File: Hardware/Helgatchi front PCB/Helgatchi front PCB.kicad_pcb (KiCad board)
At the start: 2 copper layers, 50 x 80 mm, 34 parts, among them J1 BATTERY, J2 SCREEN, M1 MOTOR, Q1 NMOS, SW1 LEFT BUTTON, SW2 CENTER BUTTON, SW3 RIGHT BUTTON, U1 XIAO ESP32-S3

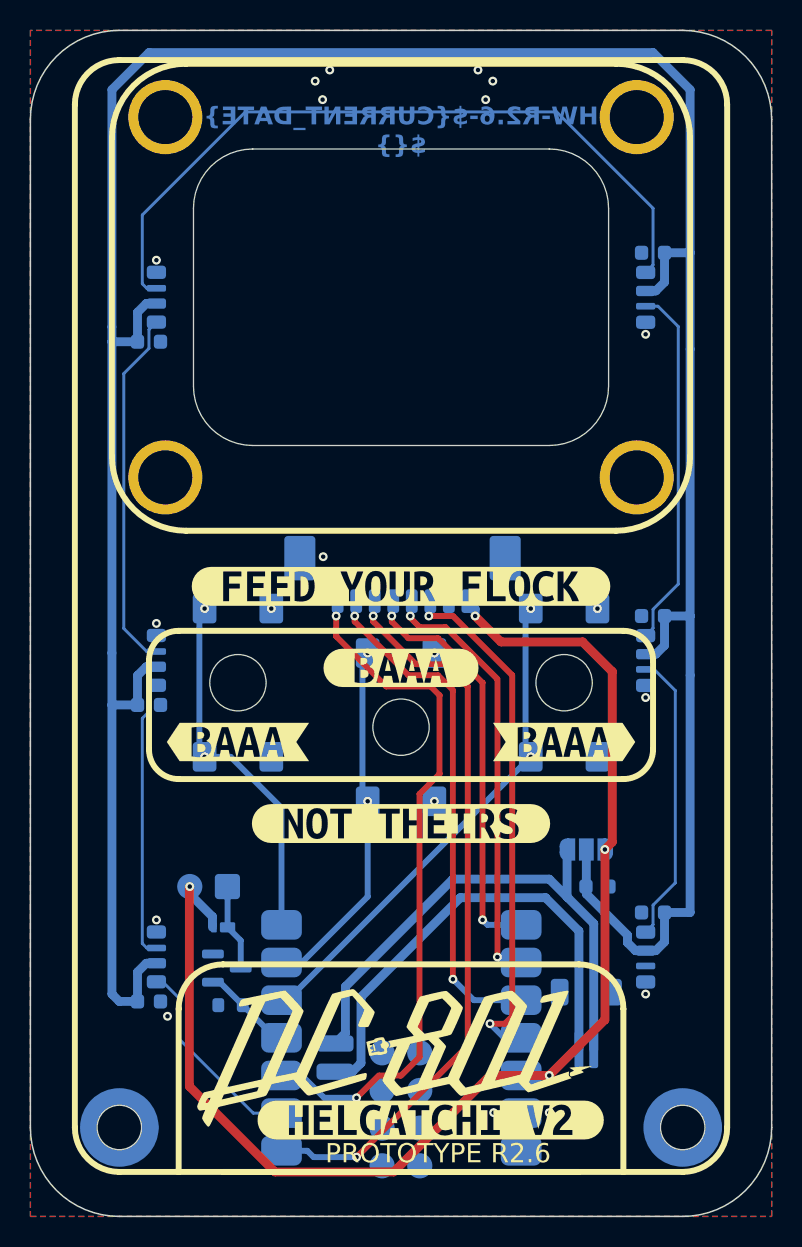
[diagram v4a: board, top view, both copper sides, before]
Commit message: R2.7
- Shifted buttons up a tiny bit
- Made room for the vibration motor to be adhered to the PCB
- Enlarged vibration motor pads for easier hand soldering
- Removed LED voltage selector (now 3.3v)
- Removed unused pins from schematic and ESP32 footprint
- Added a keepout area under ESP32
- Replaced +BATT trace
- Removed -BATT trace, tied to GND
- Added keepout around button GND vias, to prevent heat soak during soldering
- Scooted ESP back a little bit to make room for assembly
- Adjusted front silkscreen
- Swapped buttons to two GPIO Diode matrix
- Added VSENSE + resistors and capacitor
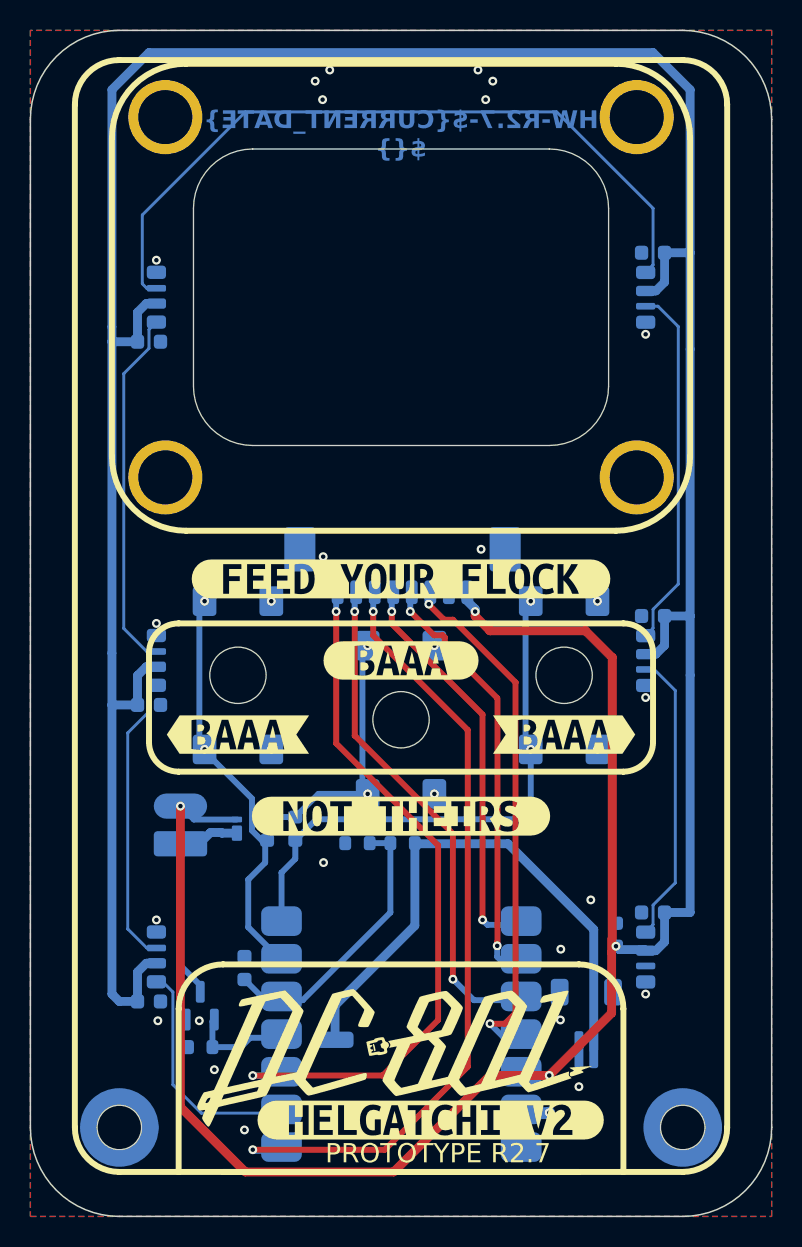
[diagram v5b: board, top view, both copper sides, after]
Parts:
- removed JP1: LEDs, Jumper:SolderJumper-3_P1.3mm_Open_RoundedPad1.0x1.5mm_NumberLabels
- added C8: 100nF, Capacitor_SMD:C_0603_1608Metric, B.Cu at (153.4, 121.7)
- added D8: D_Small, Diode_SMD:D_0603_1608Metric, B.Cu at (156.9, 112.3)
- added D9: D_Small, Diode_SMD:D_0603_1608Metric, B.Cu at (155.0, 112.3)
- added R2: 100kΩ, Resistor_SMD:R_0603_1608Metric, B.Cu at (164.1, 113.3)
- added R3: 100kΩ, Resistor_SMD:R_0603_1608Metric, B.Cu at (161.1, 113.3)
- moved D1 6.72 mm to (152.9, 112.3), turned to -90 degrees
- moved M1 5.46 mm to (149.1, 110.8), turned to 180 degrees
- moved R1 3.49 mm to (150.5, 127.1)
- moved C7 3.48 mm to (178.5, 119.5), turned to 90 degrees
- moved Q1 3.11 mm to (150.5, 124.3), turned to 90 degrees
- moved J2 0.60 mm to (164.1, 94.0)
- moved SW1 0.50 mm to (153.0, 102.0)
- moved SW2 0.50 mm to (164.0, 105.0)
- moved SW3 0.50 mm to (175.0, 102.0)
- moved kibuzzard-6976EA3A 0.50 mm to (175.0, 106.0)
- moved kibuzzard-6976EA47 0.50 mm to (153.0, 106.0)
- moved kibuzzard-6976EEFC 0.50 mm to (164.0, 95.5)
- moved kibuzzard-6976EF0C 0.50 mm to (164.0, 111.5)
- moved kibuzzard-69862DFC 0.50 mm to (164.0, 101.0)
- moved U1 0.25 mm to (164.0, 126.2)
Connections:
- C1 pad 2: LED_PWR -> +3.3V
- C2 pad 2: LED_PWR -> +3.3V
- C3 pad 2: LED_PWR -> +3.3V
- C4 pad 2: LED_PWR -> +3.3V
- C5 pad 2: LED_PWR -> +3.3V
- C6 pad 2: LED_PWR -> +3.3V
- C7 pad 1: LED_PWR -> +3.3V
- D2 pad 2: LED_PWR -> +3.3V
- D3 pad 2: LED_PWR -> +3.3V
- D4 pad 2: LED_PWR -> +3.3V
- D5 pad 2: LED_PWR -> +3.3V
- D6 pad 2: LED_PWR -> +3.3V
- D7 pad 2: LED_PWR -> +3.3V
- J1 pad 1: -BATT -> GND
- SW1 pad 2: BUTTON_LEFT -> BUTTONS_1
- SW2 pad 2: BUTTON_CENTER -> Net-(D8-K)
- SW3 pad 2: BUTTON_RIGHT -> BUTTONS_2
- U1 pad 5: BUTTON_RIGHT -> VSENSE
- U1 pad 6: BUTTON_CENTER -> BUTTONS_1
- U1 pad 7: BUTTON_LEFT -> BUTTONS_2
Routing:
- net +3.3V: track 89.3 -> 288.8 mm
- net LED_PWR: track 198.0 -> 0.00 mm
- net BUTTONS_2: track 0.00 -> 36.8 mm, vias 0 -> 2
- net BUTTON_RIGHT: track 33.9 -> 0.00 mm, vias 2 -> 0
- net -BATT: track 32.9 -> 0.00 mm
- net BUTTONS_1: track 0.00 -> 27.9 mm, vias 0 -> 2
- net BUTTON_LEFT: track 24.8 -> 0.00 mm, vias 2 -> 0
- net BUTTON_CENTER: track 24.4 -> 0.00 mm, vias 2 -> 0
- net VSENSE: track 0.00 -> 18.9 mm
- net Net-(D8-K): track 0.00 -> 17.7 mm, vias 0 -> 2
- net Net-(D1-A): track 5.96 -> 14.7 mm
- net SPI_DC: track 49.8 -> 53.0 mm
- net LED_CONTROL: track 13.7 -> 15.9 mm
- net GND: track 0.00 -> 2.01 mm, vias 16 -> 24
- net +BATT: track 36.9 -> 38.3 mm
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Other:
- board text added: "MOTOR"

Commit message: Update Helgatchi front PCB.kicad_pcb
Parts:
- moved C8 1.13 mm to (152.6, 122.5), turned to 0 degrees
- moved M1 0.62 mm to (148.5, 110.8)
- moved D1 0.43 mm to (152.5, 112.3)
- moved D9 0.36 mm to (154.6, 112.3)
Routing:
- net GND: vias 24 -> 25

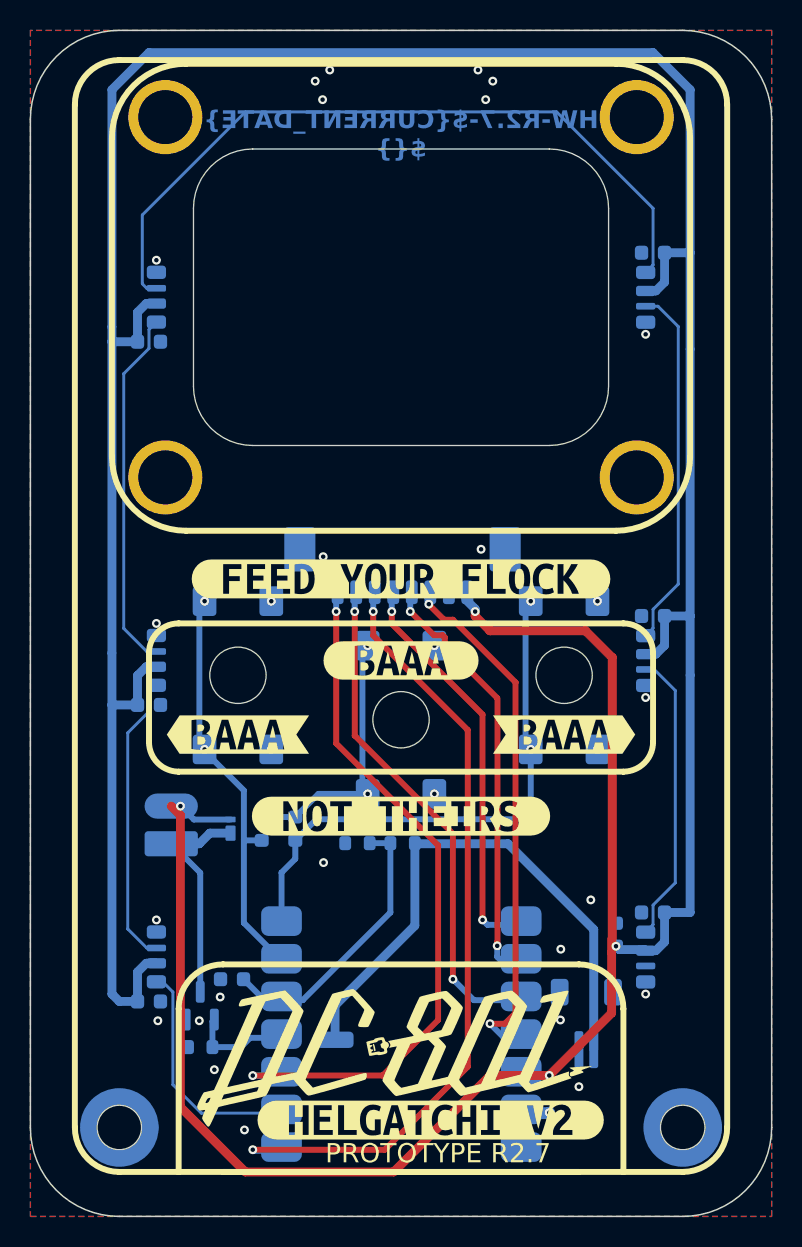
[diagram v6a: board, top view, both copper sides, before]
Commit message: Wrap up R2.7
- Added voltage sensing
- made room for Vibration buzzer
- added SMD M2 nut
- swapped flyback diode
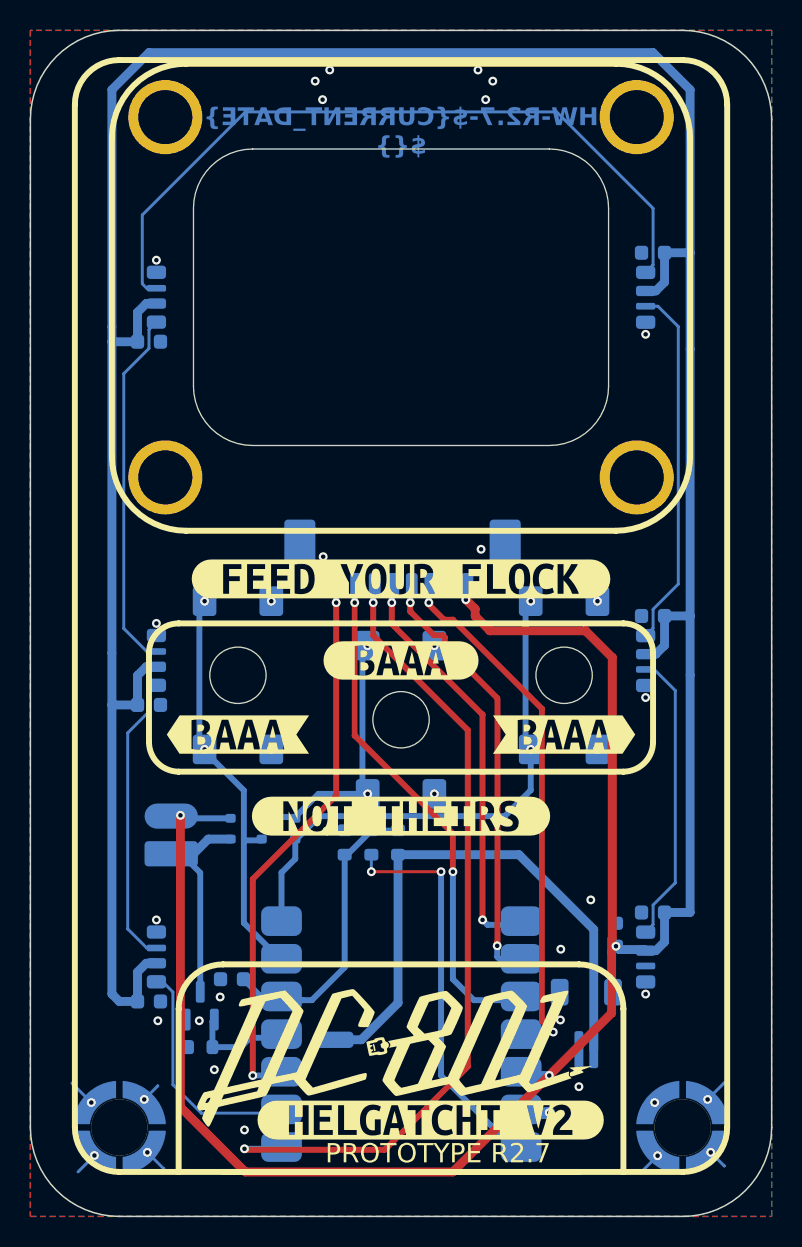
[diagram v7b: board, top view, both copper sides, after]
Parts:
- added R4: 100kΩ, Resistor_SMD:R_0603_1608Metric, B.Cu at (162.0, 113.3)
- D1: footprint SDM2U30CSP:SDM2U30CSP -> Diode_SMD:D_SOD-523
- D8, D9: value D_Small -> D_Schottky; footprint Diode_SMD:D_0603_1608Metric -> Diode_SMD:D_SOD-523
- H1, H2: value M2 -> SMTSOM225BTR; footprint Mounting_Wuerth:Mounting_Wuerth_WA-SMSI-M2_H8mm_9774080243 -> SMTSOM225BTR:SMD_BD5.6-D3.6
- moved R3 0.86 mm to (160.2, 113.3), turned to 90 degrees
- moved M1 0.68 mm to (148.5, 111.5)
- moved J2 0.50 mm to (164.1, 93.5)
- moved R2 0.31 mm to (163.8, 113.3), turned to 90 degrees
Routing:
- net +5V: track 0.00 -> 27.0 mm, vias 0 -> 2
- net GND: track 2.01 -> 27.3 mm, vias 25 -> 39
- net (no net): track 14.5 -> 0.00 mm, vias 6 -> 0
- net SPI_BL: track 47.3 -> 37.5 mm
- net SPI_DC: track 53.0 -> 55.1 mm
- net VSENSE: track 19.0 -> 20.2 mm
- net SPI_SCK: track 28.7 -> 29.8 mm
- net SPI_RES: track 33.6 -> 34.7 mm
- net SPI_CS: track 27.0 -> 28.0 mm
- net SPI_MOSI: track 35.3 -> 36.3 mm
- net BUTTONS_2: track 36.8 -> 36.2 mm
